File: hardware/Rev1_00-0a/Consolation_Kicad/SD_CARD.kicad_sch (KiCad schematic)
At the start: 12 parts, among them J1 0484050003, U3 AP2192AFGEG-7

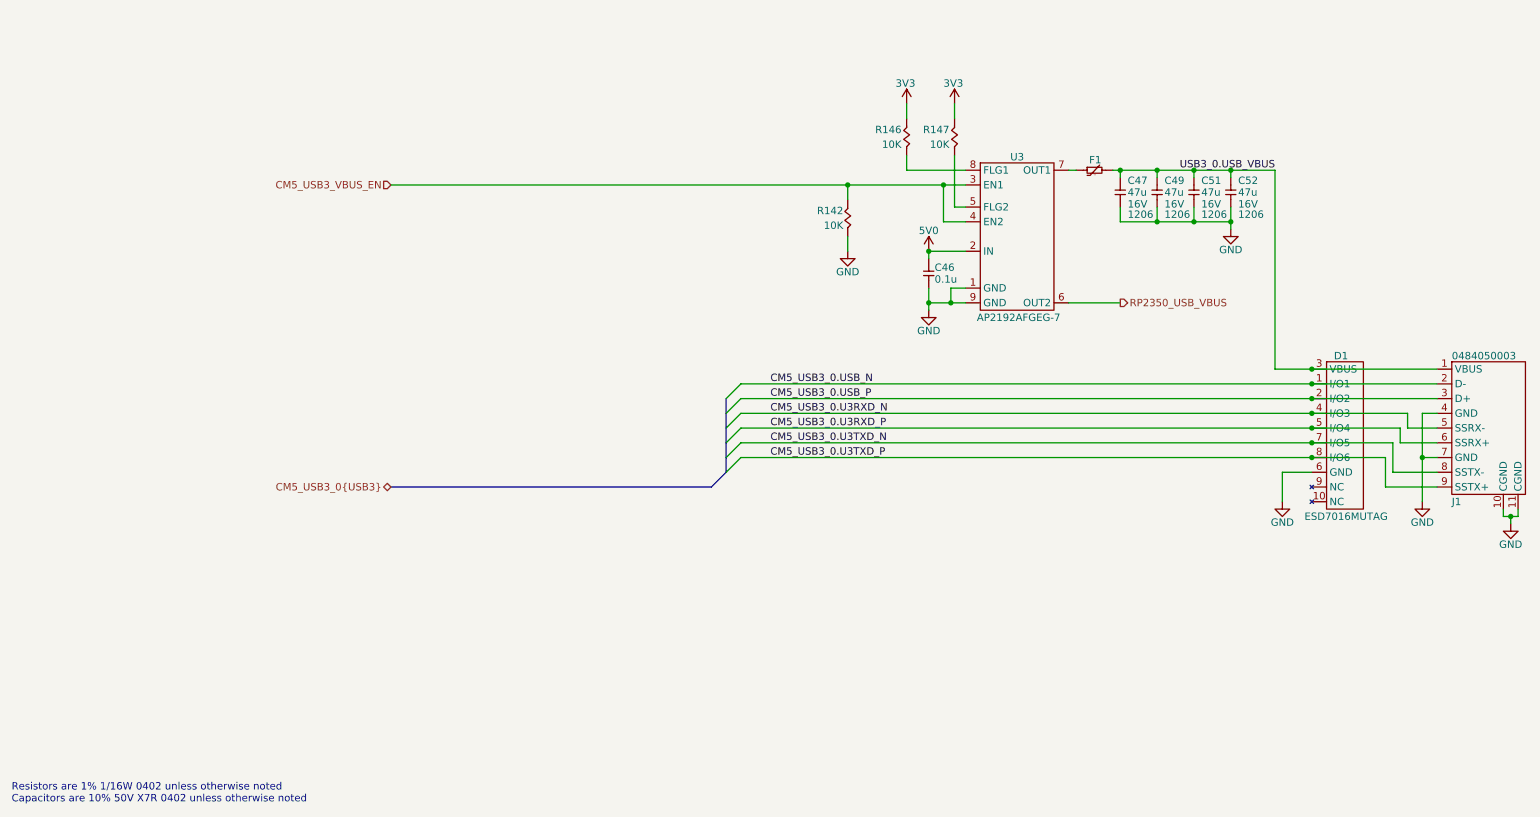
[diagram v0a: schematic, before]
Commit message: ConJoy mostly ready for alpha prototype. Confirm few other potential tweaks at 3d printing
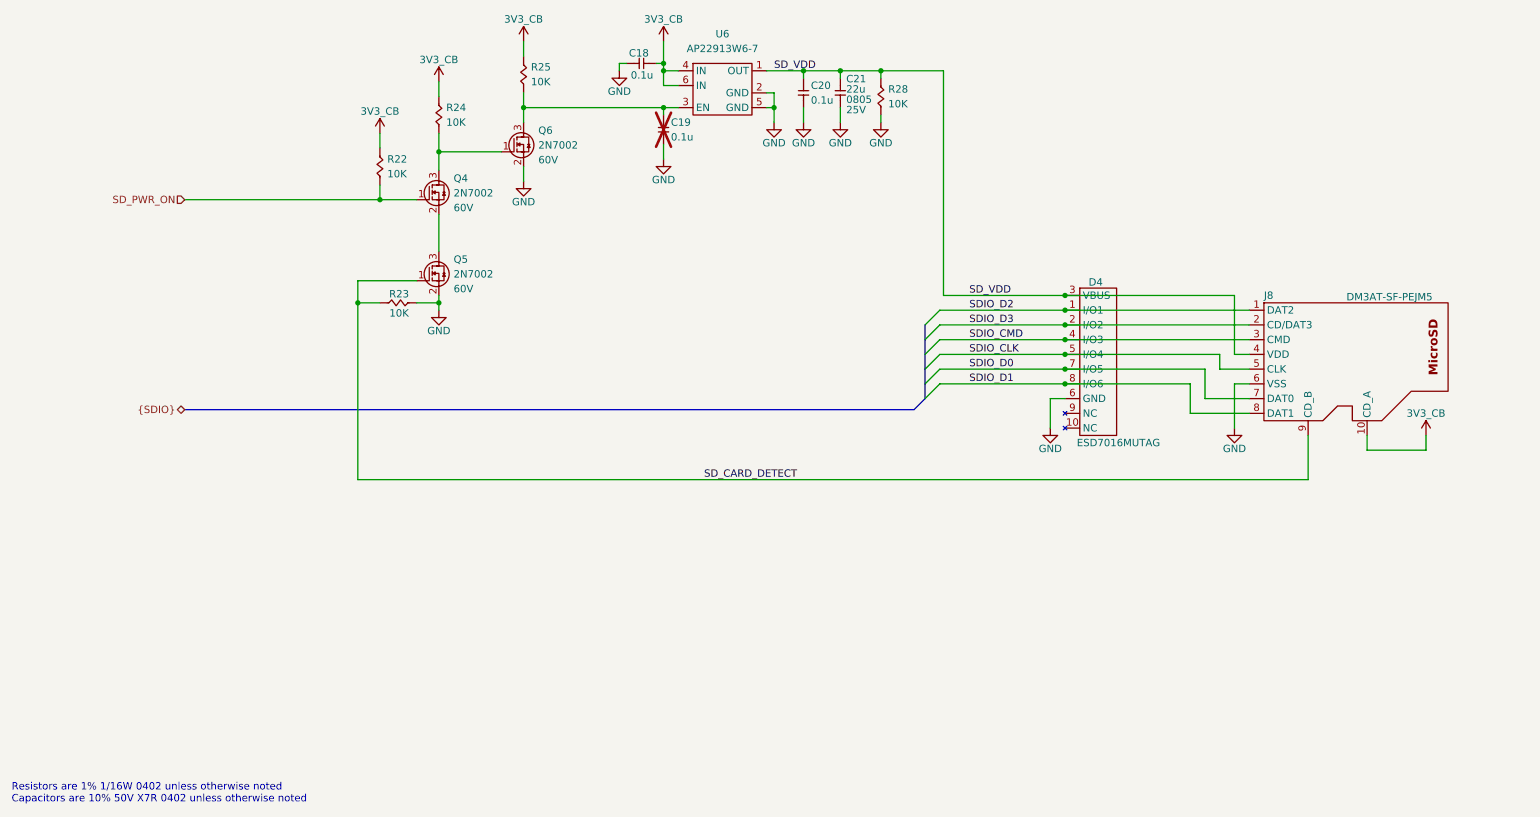
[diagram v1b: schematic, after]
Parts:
- removed C46: 0.1u, footprint:CAP_NONPOL_0402, symbol KicadCompDb:Capacitors/CAP_CER_SMT_00001
- removed C47, C49, C51, C52: 47u, footprint:CAP_NONPOL_1206, symbol KicadCompDb:Capacitors/CAP_CER_SMT_00010
- removed D1: ESD7016MUTAG, footprint:UDFN8, symbol KicadCompDb:ESD Diodes/ESD_DIODE_00001
- removed F1: MINISMDC050F-2, footprint:PTC_1812, symbol KicadCompDb:PTC Resettable fuse/PTC_00001
- removed J1: 0484050003, footprint:0484050003, symbol KicadCompDb:Connector/CONN_00009
- removed R142, R146, R147: 10K, footprint:RES_0402, symbol KicadCompDb:Resistors/RES_SMT_00013
- removed U3: AP2192AFGEG-7, footprint:U-DFN3030-8, symbol KicadCompDb:Load Switch/LOAD_SW_00002
- added C18, C19, C20: 0.1u, footprint:CAP_NONPOL_0402, symbol KicadCompDb:Capacitors/CAP_CER_SMT_00001
- added C21: 22u, footprint:CAP_NONPOL_0805, symbol KicadCompDb:Capacitors/CAP_CER_SMT_00011
- added D4: ESD7016MUTAG, footprint:UDFN8, symbol KicadCompDb:ESD Diodes/ESD_DIODE_00001
- added J8: DM3AT-SF-PEJM5, footprint:DM3AT-SF-PEJM5, symbol KicadCompDb:Connector/CONN_00008
- added Q4, Q5, Q6: 2N7002, footprint:SOT-23-3, symbol KicadCompDb:Mosfet/MOSFET_00001
- added R22, R23, R24, R25, R28: 10K, footprint:RES_0402, symbol KicadCompDb:Resistors/RES_SMT_00013
- added U6: AP22913W6-7, footprint:SOT-23-6, symbol KicadCompDb:Load Switch/LOAD_SW_00001
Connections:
- net GND: now also C18.1, C19.1, C20.1, C21.1, D4.6 (GND), J8.6 (VSS), Q5.2 (S), Q6.2 (S), R23.1, R28.1, U6.2 (GND), U6.5 (GND)
- new net: Q4.3 (D), Q6.1 (G), R24.1
- new net: C19.2, Q6.3 (D), R25.1, U6.3 (EN)
- new net: Q4.2 (S), Q5.3 (D)
- new net 3V3_CB: C18.2, J8.10 (CD_A), R22.2, R24.2, R25.2, U6.4 (IN), U6.6 (IN)
- new net SDIO_CLK: D4.5 (I/O4), J8.5 (CLK)
- new net SDIO_CMD: D4.4 (I/O3), J8.3 (CMD)
- new net SDIO_D0: D4.7 (I/O5), J8.7 (DAT0)
- new net SDIO_D1: D4.8 (I/O6), J8.8 (DAT1)
- new net SDIO_D2: D4.1 (I/O1), J8.1 (DAT2)
- new net SDIO_D3: D4.2 (I/O2), J8.2 (CD/DAT3)
- new net SD_CARD_DETECT: J8.9 (CD_B), Q5.1 (G), R23.2
- new net SD_PWR_ON: Q4.1 (G), R22.1
- new net SD_VDD: C20.2, C21.2, D4.3 (VBUS), J8.4 (VDD), R28.2, U6.1 (OUT)

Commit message: Major update to consolation schematics to include - Power supply - RESET SUPERVISOR - Review of GPIO and pinmux
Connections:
- net 3V3_CB renamed 3V3
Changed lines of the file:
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@@
 	(title_block
 		(title "Consolation [Console Emulation]")
-		(date "2026-08-03")
-		(rev "1.00-0a")
+		(date "2026-08-08")
+		(rev "1.00-0A")
 		(comment 1 "Jean-Francois Bilodeau")
 		(comment 2 "P.Eng #6022173")
@@
 			)
 		)
-		(property "Value" "3V3_CB"
+		(property "Value" "3V3"
 			(at 76.2 53.34 0)
 			(show_name no)
@@
 			)
 		)
-		(property "Value" "3V3_CB"
+		(property "Value" "3V3"
 			(at 86.36 44.45 0)
 			(show_name no)
@@
 			)
 		)
-		(property "Value" "3V3_CB"
+		(property "Value" "3V3"
 			(at 256.54 105.41 0)
 			(show_name no)
@@
 			)
 		)
-		(property "Value" "3V3_CB"
+		(property "Value" "3V3"
 			(at 125.095 37.465 0)
 			(show_name no)
@@
 			)
 		)
-		(property "Value" "3V3_CB"
+		(property "Value" "3V3"
 			(at 100.965 37.465 0)
 			(show_name no)

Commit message: Removed unnecessary functions (USB2 mux, CapTouch) Adjusted 220uF alum capacitor for codec (slimmer version)
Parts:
- removed Q4, Q5, Q6: 2N7002, footprint:SOT-23-3, symbol KicadCompDb:Mosfet/MOSFET_00001
- added Q23, Q24, Q25: SSM3K56FS,LF, footprint:SC-75, symbol KicadCompDb:Mosfet/MOSFET_00002
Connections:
- net GND: now also Q24.2 (S), Q25.2 (S)
- net SD_CARD_DETECT: now also Q25.1 (G)
- net SD_PWR_ON: now also Q23.1 (G)
- net at R24.1: now also Q23.3 (D), Q24.1 (G)
- net at C19.2, R25.1, U6.3 (EN): now also Q24.3 (D)
- new net: Q23.2 (S), Q25.3 (D)

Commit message: Component preliminary placement
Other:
- moved on the sheet: C19
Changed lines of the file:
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@@
 		(in_pos_files yes)
 		(dnp no)
-		(fields_autoplaced yes)
 		(property "Reference" "U6"
-			(at 135.255 40.005 0)
+			(at 135.128 44.196 0)
 			(show_name no)
 			(do_not_autoplace no)
@@
 		)
 		(property "Value" "AP22913W6-7"
-			(at 135.255 42.545 0)
+			(at 135.128 55.118 0)
 			(show_name no)
 			(do_not_autoplace no)
@@
 	(symbol
 		(lib_id "KicadCompDb:Capacitors/CAP_CER_SMT_00001")
-		(at 125.095 59.055 90)
+		(at 125.095 59.055 270)
+		(mirror x)
 		(unit 1)
 		(body_style 1)
@@
 		(dnp yes)
 		(property "Reference" "C19"
-			(at 126.365 55.245 90)
+			(at 123.825 55.245 90)
 			(show_name no)
 			(do_not_autoplace no)
@@
 		)
 		(property "Value" "0.1u"
-			(at 126.365 57.785 90)
+			(at 123.825 57.785 90)
 			(show_name no)
 			(do_not_autoplace no)
@@
 		)
 		(property "Footprint" "footprint:CAP_NONPOL_0402"
-			(at 147.193 58.547 0)
+			(at 102.997 58.547 0)
 			(hide yes)
 			(show_name no)
@@
 		)
 		(property "Description" "CAP CER 0.1UF 50V X7R 0402"
-			(at 135.001 57.277 0)
+			(at 115.189 57.277 0)
 			(hide yes)
 			(show_name no)
@@
 		)
 		(property "Tolerance" "±10%"
-			(at 145.415 58.801 0)
+			(at 104.775 58.801 0)
 			(hide yes)
 			(show_name no)
@@
 		)
 		(property "Dielectric" "X7R"
-			(at 139.319 58.801 0)
+			(at 110.871 58.801 0)
 			(hide yes)
 			(show_name no)
@@
 		)
 		(property "Package" "0402"
-			(at 141.351 59.055 0)
+			(at 108.839 59.055 0)
 			(hide yes)
 			(show_name no)
@@
 		)
 		(property "Operating Temperature" "-55°C ~ 125°C"
-			(at 149.479 58.293 0)
+			(at 100.711 58.293 0)
 			(hide yes)
 			(show_name no)
@@
 		)
 		(property "Manufacturer" "Murata Electronics"
-			(at 143.383 58.801 0)
+			(at 106.807 58.801 0)
 			(hide yes)
 			(show_name no)
@@
 		)
 		(property "Manufacturer Part Number" "GRM155R71H104KE14D"
-			(at 132.969 58.801 0)
+			(at 117.221 58.801 0)
 			(hide yes)
 			(show_name no)
@@
 		)
 		(property "Distributor" "DigiKey"
-			(at 130.937 59.055 0)
+			(at 119.253 59.055 0)
 			(hide yes)
 			(show_name no)
@@
 		)
 		(property "Distributor Part Number" "490-10700-1-ND"
-			(at 137.287 58.293 0)
-			(hide yes)
-			(show_name no)
+			(at 112.903 58.293 0)
+			(hide yes)
+			(show_name no)

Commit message: Update ConJoy L2 trigger (2-level trigger instead) Update ConJoy all output files accordingly
Work on Consolation preliminary placement
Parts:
- removed C19: 0.1u, footprint:CAP_NONPOL_0402, symbol KicadCompDb:Capacitors/CAP_CER_SMT_00001
- added D27: ESD7351HT1G, footprint:SOD-323, symbol KicadCompDb:ESD Diodes/ESD_DIODE_00006
- added R119: 22R, footprint:RES_0402, symbol KicadCompDb:Resistors/RES_SMT_00015
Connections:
- net GND: now also D4.3 (VBUS), D27.2 (A)
- net SD_CARD_DETECT: now also D27.1 (K), R119.2; no longer J8.9 (CD_B)
- net SD_VDD: no longer D4.3 (VBUS)
- new net: J8.9 (CD_B), R119.1

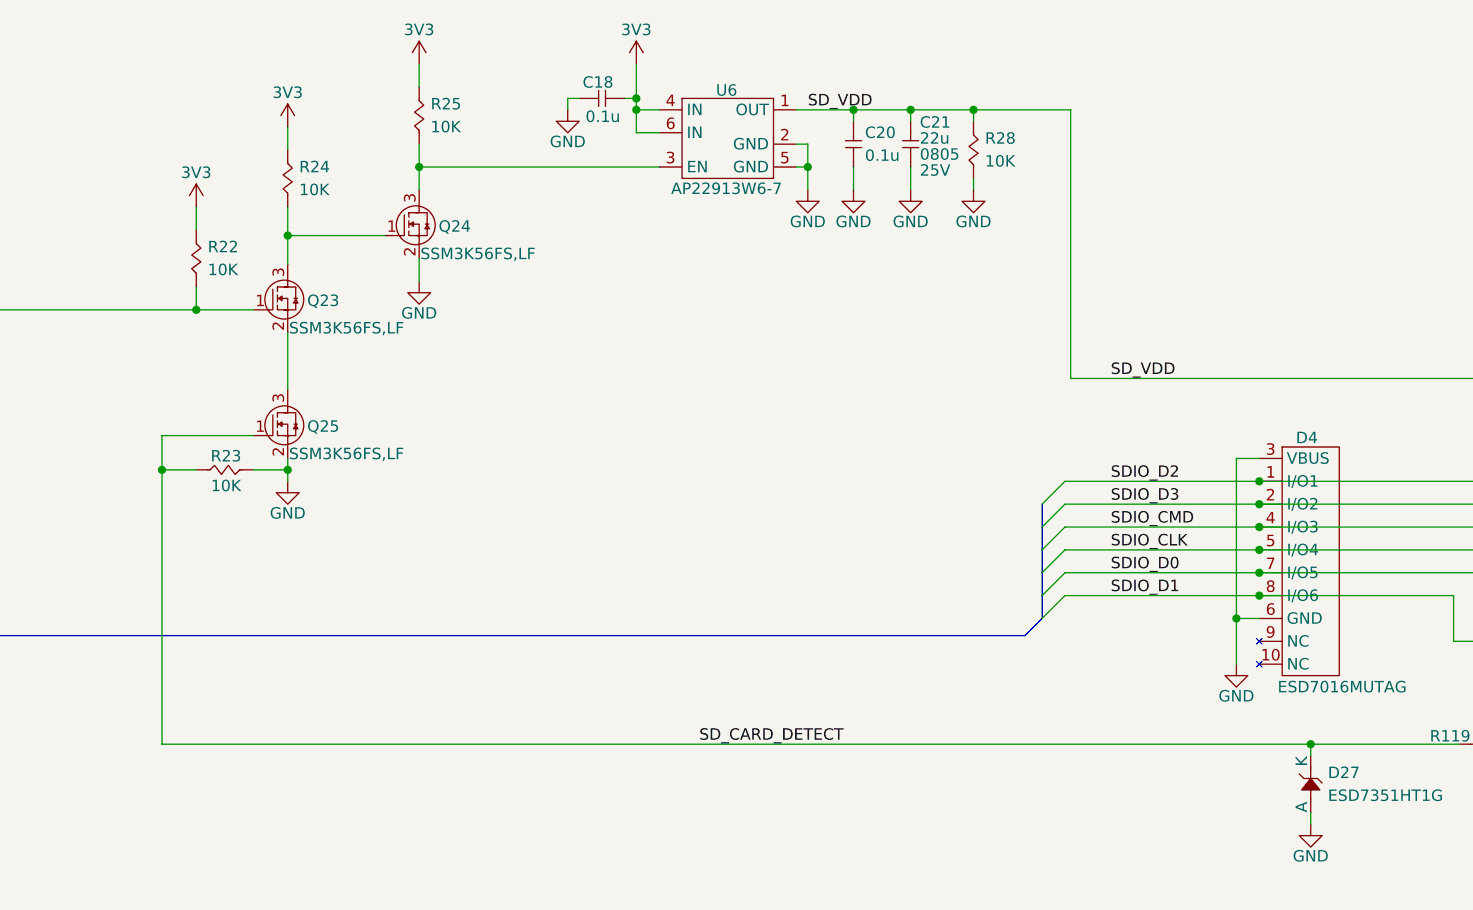
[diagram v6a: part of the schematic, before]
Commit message: Preliminary placement done Add test points to PCB
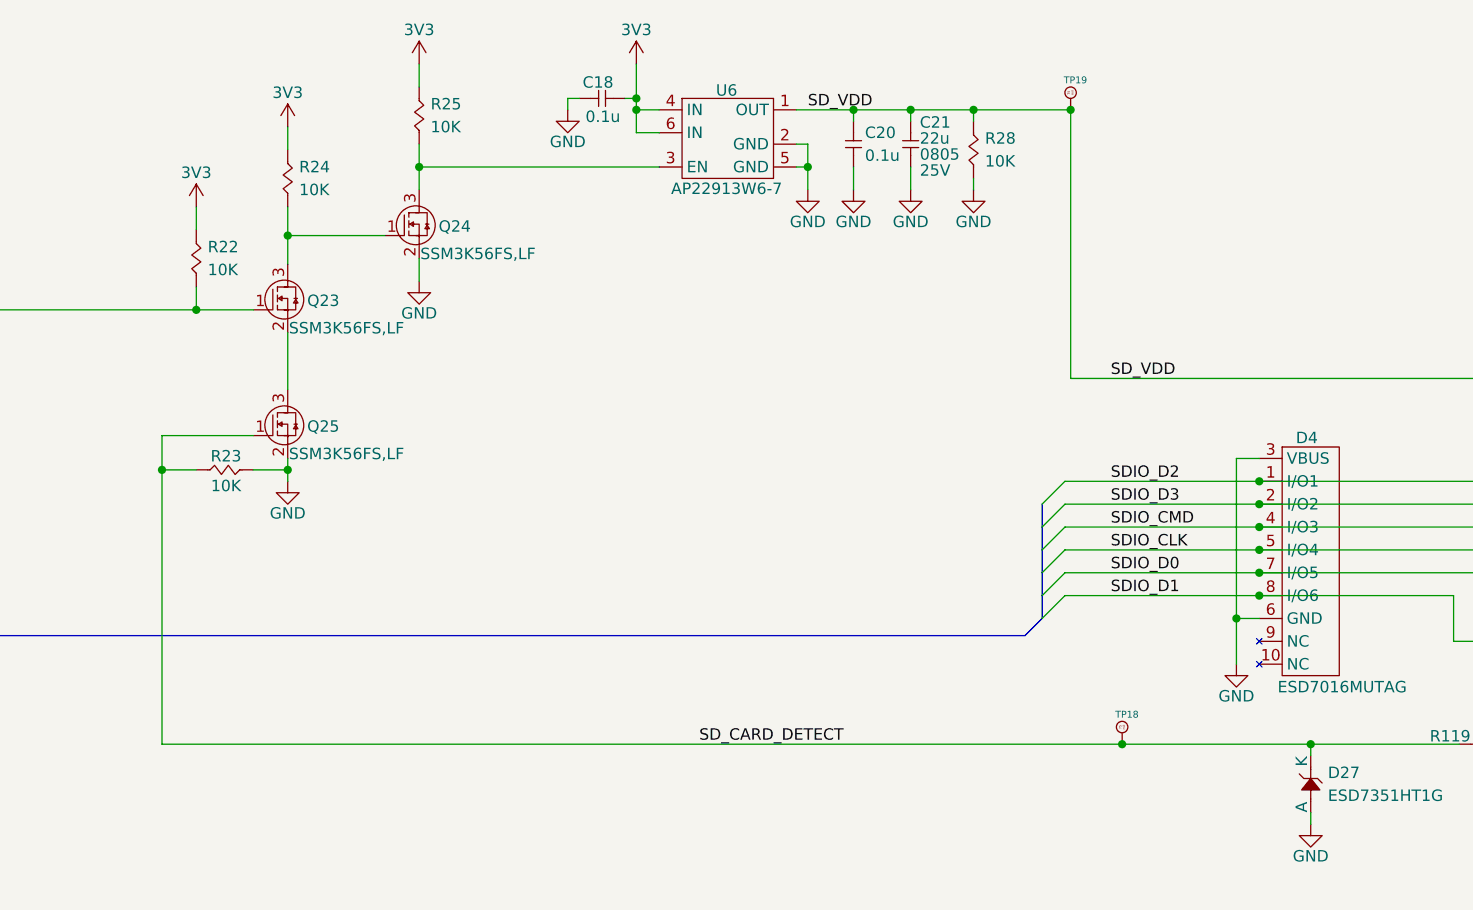
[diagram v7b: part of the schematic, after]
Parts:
- added TP18, TP19: 75 mils, footprint:SMT_TP_75_MILS, symbol KicadCompDb:Test Point/TP_00004
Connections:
- net SD_CARD_DETECT: now also TP18.1
- net SD_VDD: now also TP19.1
